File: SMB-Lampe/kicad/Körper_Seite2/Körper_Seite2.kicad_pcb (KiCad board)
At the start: 2 copper layers, 121.9 x 96.3 mm, 28 parts, among them J1 Conn_01x01_Pin, J2 Conn_01x01_Pin, J3 Conn_01x01_Pin

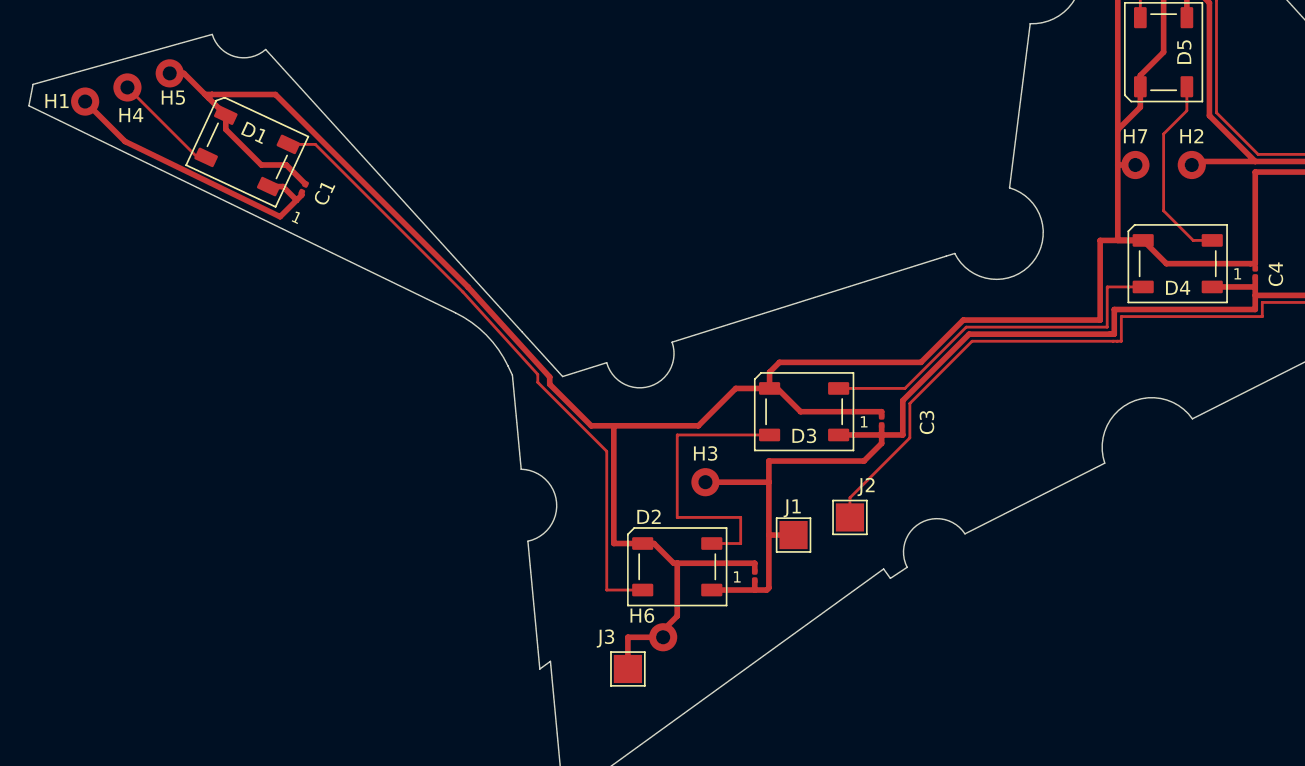
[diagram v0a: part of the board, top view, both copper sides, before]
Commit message: Vorderes Hinterbein fertig
Alle Platinen sind fertig beschaltet
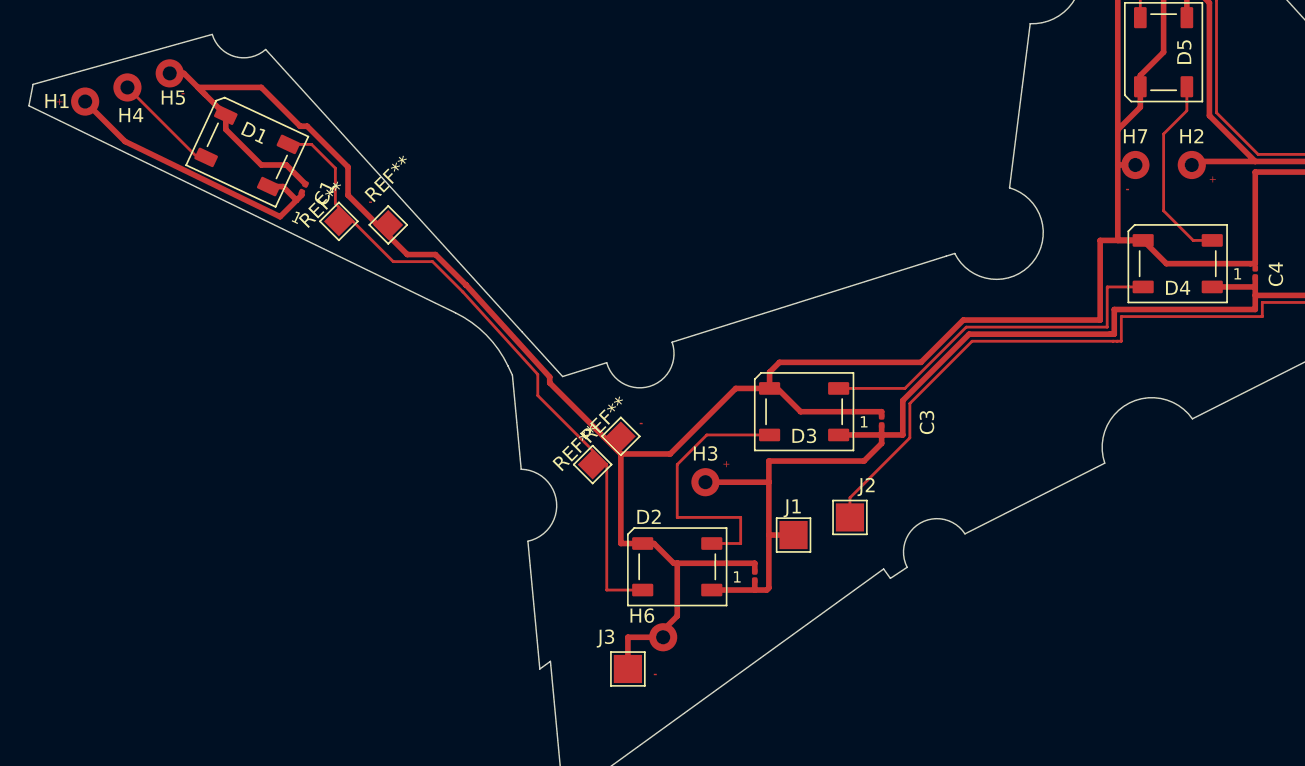
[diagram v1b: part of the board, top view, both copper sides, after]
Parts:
- added REF**: TestPoint_Pad_1.5x1.5mm, TestPoint:TestPoint_Pad_1.5x1.5mm, F.Cu at (110.0, 114.8)
- added REF**: TestPoint_Pad_1.5x1.5mm, TestPoint:TestPoint_Pad_1.5x1.5mm, F.Cu at (112.0, 112.8)
- added REF**: TestPoint_Pad_1.5x1.5mm, TestPoint:TestPoint_Pad_1.5x1.5mm, F.Cu at (95.5, 97.8)
- added REF**: TestPoint_Pad_1.5x1.5mm, TestPoint:TestPoint_Pad_1.5x1.5mm, F.Cu at (92.0, 97.5)
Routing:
- net GND: track 348.7 -> 350.4 mm
- net Net-(D1-DOUT): track 44.5 -> 46.0 mm
- net Net-(D2-DOUT): track 20.8 -> 19.6 mm
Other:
- board text added: "+"
- board text added: "-"

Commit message: Hinterbeine Geändert teilweiße Körper
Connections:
- REF** pad 1: (no net) -> Net-(D1-DOUT)
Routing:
- net (no net): track 0.00 -> 3.40 mm
- net Net-(D7-DOUT): track 80.2 -> 82.5 mm
- net GND: track 350.4 -> 351.6 mm
- net Net-(D2-DOUT): track 19.6 -> 20.1 mm
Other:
- outline, holes or cut-outs redrawn
- board text removed: "-"

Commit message: Alle Platinen sind fertig zur Fertigung
Aus diesem Stand folgt das erste fertig leuchtende Pferd
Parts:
- C1, C2, C3, C4, C5, C6, C7, C8, C9: footprint Capacitor_SMD:C_0201_0603Metric -> Capacitor_SMD:C_0603_1608Metric_Pad1.08x0.95mm_HandSolder
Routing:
- net GND: track 351.6 -> 358.0 mm
- net Net-(D8-DOUT): track 34.9 -> 37.5 mm
- net +5V: track 207.2 -> 209.1 mm
- net Net-(D7-DOUT): track 82.5 -> 80.9 mm
- net /Data_OUT_Hinterbein_vorne_Seite1: track 71.5 -> 72.8 mm
- net (no net): track 3.40 -> 2.50 mm
- net Net-(D1-DOUT): track 45.8 -> 46.5 mm
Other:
- board size 121.9 x 96.3 mm -> 281.3 x 135.5 mm

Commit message: Nachträgliche Änderungen für die Fertigung und Präsentation
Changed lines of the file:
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@@
 		(tags "LED RGB NeoPixel PLCC-4 5050")
 		(property "Reference" "D6"
-			(at 0 -2.12132 45)
+			(at 0 4.242641 45)
 			(layer "F.SilkS")
 			(effects
@@
 		(tags "capacitor handsolder")
 		(property "Reference" "C2"
-			(at 0 -1.43 90)
+			(at 0 2 90)
 			(layer "F.SilkS")
 			(effects
@@
 		(tags "LED RGB NeoPixel PLCC-4 5050")
 		(property "Reference" "D9"
-			(at 0.146747 1.513594 75)
+			(at 4.57081 -2.260021 75)
 			(layer "F.SilkS")
 			(effects
@@
 		(tags "capacitor handsolder")
 		(property "Reference" "C6"
-			(at 0 -1.43 135)
+			(at 0 2.12132 135)
 			(layer "F.SilkS")
 			(effects
@@
 		(tags "capacitor handsolder")
 		(property "Reference" "C1"
-			(at 0 -1.43 65)
+			(at 0.321251 1.505265 65)
 			(layer "F.SilkS")
 			(effects
@@
 		(tags "capacitor handsolder")
 		(property "Reference" "C3"
-			(at 0 -1.43 90)
+			(at 0 2 90)
 			(layer "F.SilkS")
 			(effects
@@
 		(tags "LED RGB NeoPixel PLCC-4 5050")
 		(property "Reference" "D8"
-			(at 0.148507 -1.266075 18)
+			(at 5.206805 -1.462593 18)
 			(layer "F.SilkS")
 			(effects
@@
 		(tags "capacitor handsolder")
 		(property "Reference" "C8"
-			(at 0.391225 1.546591 288)
+			(at 0.172513 1.896112 288)
 			(layer "F.SilkS")
 			(effects
@@
 		(tags "LED RGB NeoPixel PLCC-4 5050")
 		(property "Reference" "D4"
-			(at 0 -1.75 0)
+			(at 0 -4.5 0)
 			(layer "F.SilkS")
 			(effects
@@
 		(tags "LED RGB NeoPixel PLCC-4 5050")
 		(property "Reference" "D3"
-			(at 0 -1.75 0)
+			(at 0 4 0)
 			(layer "F.SilkS")
 			(effects
@@
 			(at 2.298097 -2.298097 45)
 			(layer "F.SilkS")
+			(hide yes)
 			(effects
 				(font
@@
 		(tags "LED RGB NeoPixel PLCC-4 5050")
 		(property "Reference" "D5"
-			(at 0 -1.5 90)
+			(at 0 4.5 90)
 			(layer "F.SilkS")
 			(effects
@@
 		(tags "LED RGB NeoPixel PLCC-4 5050")
 		(property "Reference" "D1"
-			(at 0.075119 1.344194 155)
+			(at 0.119702 3.806005 155)
 			(layer "F.SilkS")
 			(effects
@@
 			(at 0 -1.648 45)
 			(layer "F.SilkS")
+			(hide yes)
 			(effects
 				(font
@@
 		(tags "capacitor handsolder")
 		(property "Reference" "C9"
-			(at 0 -1.43 0)
+			(at 0 2 0)
 			(layer "F.SilkS")
 			(effects
@@
 		(tags "LED RGB NeoPixel PLCC-4 5050")
 		(property "Reference" "D7"
-			(at 0.049953 -1.456882 151)
+			(at 0.052406 -4.030788 151)
 			(layer "F.SilkS")
 			(effects
